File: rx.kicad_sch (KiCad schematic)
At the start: 33 parts, among them U1 CC1200

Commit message: MPN/PN update
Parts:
- C5: MPN (none) -> C0603C473K5RACTU
- C5: MPN (none) -> GRM1885C1H152JA01D
- C5: MPN (none) -> C0603C223K4RACTU
- C5: MPN (none) -> GRM1885C1H9R1BA01D
- C5: MPN (none) -> CC0603CRNPO9BN5R1
- C5: MPN (none) -> C0603C103K5RAC7081
- C5: MPN (none) -> C0603C104M5RAC7411
- C5: MPN (none) -> GRM1885C1H6R2BA01D
- FB1: MPN (none) -> BLM18KG601SH1D
- JP1, TP5: MPN (none) -> -
- L3: MPN (none) -> LQW18AS15NG00D; PN (none) -> LQW18AS15NG00D
- L3: MPN (none) -> LQW18AN27NG00D; PN (none) -> LQW18AN27NG00D
- L3: MPN (none) -> LQW18AN22NG00D; PN (none) -> LQW18AN22NG00D
- L3: MPN (none) -> LQW18AS56NG00D; PN (none) -> LQW18AS56NG00D
- R2: MPN (none) -> CRCW0603100RFKECC; PN (none) -> CRCW0603100RFKECC
- R2: MPN (none) -> CRGCQ0603F56K; PN (none) -> CRGCQ0603F56K
- U1: MPN (none) -> CC1200RHBR
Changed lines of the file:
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@@
+      (effects (font (size 1.27 1.27)) hide)
+    )
+    (property "MPN" "LQW18AS15NG00D" (at 228.6 134.62 0)
+      (effects (font (size 1.27 1.27)) hide)
+    )
+    (property "PN" "LQW18AS15NG00D" (at 228.6 134.62 0)
       (effects (font (size 1.27 1.27)) hide)
     )
@@
       (effects (font (size 1.27 1.27)) hide)
     )
+    (property "MPN" "C0603C473K5RACTU" (at 177.8 205.74 0)
+      (effects (font (size 1.27 1.27)) hide)
+    )
     (pin "1")
     (pin "2")
@@
       (effects (font (size 1.27 1.27)) hide)
     )
+    (property "MPN" "LQW18AN27NG00D" (at 213.36 128.27 0)
+      (effects (font (size 1.27 1.27)) hide)
+    )
+    (property "PN" "LQW18AN27NG00D" (at 213.36 128.27 0)
+      (effects (font (size 1.27 1.27)) hide)
+    )
     (pin "1")
     (pin "2")
@@
       (effects (font (size 1.27 1.27)) hide)
     )
+    (property "MPN" "C0603C473K5RACTU" (at 124.46 205.74 0)
+      (effects (font (size 1.27 1.27)) hide)
+    )
     (pin "1")
     (pin "2")
@@
     )
     (property "PN" "GRM1885C1H152JA01D" (at 152.4 106.68 0)
+      (effects (font (size 1.27 1.27)) hide)
+    )
+    (property "MPN" "GRM1885C1H152JA01D" (at 152.4 106.68 0)
       (effects (font (size 1.27 1.27)) hide)
     )
@@
       (effects (font (size 1.27 1.27)) hide)
     )
+    (property "MPN" "C0603C223K4RACTU" (at 247.65 101.6 0)
+      (effects (font (size 1.27 1.27)) hide)
+    )
     (pin "1")
     (pin "2")
@@
       (effects (font (size 1.27 1.27)) hide)
     )
+    (property "MPN" "C0603C473K5RACTU" (at 160.02 205.74 0)
+      (effects (font (size 1.27 1.27)) hide)
+    )
     (pin "1")
     (pin "2")
@@
       (effects (font (size 1.27 1.27)) hide)
     )
+    (property "MPN" "C0603C473K5RACTU" (at 195.58 205.74 0)
+      (effects (font (size 1.27 1.27)) hide)
+    )
     (pin "1")
     (pin "2")
@@
       (effects (font (size 1.27 1.27)) hide)
     )
+    (property "MPN" "-" (at 204.47 68.58 0)
+      (effects (font (size 1.27 1.27)) hide)
+    )
     (pin "1")
     (pin "2")
@@
       (effects (font (size 1.27 1.27)) hide)
     )
+    (property "MPN" "C0603C473K5RACTU" (at 219.71 101.6 0)
+      (effects (font (size 1.27 1.27)) hide)
+    )
     (pin "1")
     (pin "2")
@@
       (effects (font (size 1.27 1.27)) hide)
     )
+    (property "MPN" "GRM1885C1H9R1BA01D" (at 152.4 93.98 0)
+      (effects (font (size 1.27 1.27)) hide)
+    )
     (pin "1")
     (pin "2")
@@
       (effects (font (size 1.27 1.27)) hide)
     )
+    (property "MPN" "CC0603CRNPO9BN5R1" (at 203.2 128.27 0)
+      (effects (font (size 1.27 1.27)) hide)
+    )
     (pin "1")
     (pin "2")
@@
       (effects (font (size 1.27 1.27)) hide)
     )
+    (property "MPN" "LQW18AN22NG00D" (at 247.65 134.62 0)
+      (effects (font (size 1.27 1.27)) hide)
+    )
+    (property "PN" "LQW18AN22NG00D" (at 247.65 134.62 0)
+      (effects (font (size 1.27 1.27)) hide)
+    )
     (pin "1")
     (pin "2")
@@
       (effects (font (size 1.27 1.27)) hide)
     )
+    (property "MPN" "C0603C473K5RACTU" (at 186.69 205.74 0)
+      (effects (font (size 1.27 1.27)) hide)
+    )
     (pin "1")
     (pin "2")
@@
       (effects (font (size 1.27 1.27)) hide)
     )
+    (property "MPN" "C0603C473K5RACTU" (at 142.24 205.74 0)
+      (effects (font (size 1.27 1.27)) hide)
+    )
     (pin "1")
     (pin "2")
@@
       (effects (font (size 1.27 1.27)) hide)
     )
+    (property "MPN" "C0603C473K5RACTU" (at 133.35 205.74 0)
+      (effects (font (size 1.27 1.27)) hide)
+    )
     (pin "1")
     (pin "2")
@@
       (effects (font (size 1.27 1.27)) hide)
     )
+    (property "MPN" "C0603C103K5RAC7081" (at 237.49 101.6 0)
+      (effects (font (size 1.27 1.27)) hide)
+    )
     (pin "1")
     (pin "2")
@@
       (effects (font (size 1.27 1.27)) hide)
     )
+    (property "MPN" "CC0603CRNPO9BN5R1" (at 219.71 127 0)
+      (effects (font (size 1.27 1.27)) hide)
+    )
     (pin "1")
     (pin "2")
@@
       (effects (font (size 1.27 1.27)) hide)
     )
-    (property "PN" "" (at 152.4 71.12 0)
+    (property "PN" "CRCW0603100RFKECC" (at 152.4 71.12 0)
+      (effects (font (size 1.27 1.27)) hide)
+    )
+    (property "MPN" "CRCW0603100RFKECC" (at 152.4 71.12 0)
       (effects (font (size 1.27 1.27)) hide)
     )
@@
       (effects (font (size 1.27 1.27)) hide)
     )
-    (property "PN" "" (at 152.4 73.66 0)
+    (property "PN" "CRCW0603100RFKECC" (at 152.4 73.66 0)
+      (effects (font (size 1.27 1.27)) hide)
+    )
+    (property "MPN" "CRCW0603100RFKECC" (at 152.4 73.66 0)
       (effects (font (size 1.27 1.27)) hide)
     )
@@
       (effects (font (size 1.27 1.27)) hide)
     )
+    (property "MPN" "C0603C104M5RAC7411" (at 207.01 205.74 0)
+      (effects (font (size 1.27 1.27)) hide)
+    )
     (pin "1")
     (pin "2")
@@
       (effects (font (size 1.27 1.27)) hide)
     )
+    (property "MPN" "C0603C473K5RACTU" (at 168.91 205.74 0)
+      (effects (font (size 1.27 1.27)) hide)
+    )
     (pin "1")
     (pin "2")
@@
       (effects (font (size 1.27 1.27)) hide)
     )
+    (property "MPN" "CC0603CRNPO9BN5R1" (at 237.49 134.62 0)
+      (effects (font (size 1.27 1.27)) hide)
+    )
     (pin "1")
     (pin "2")
@@
       (effects (font (size 1.27 1.27)) hide)
     )
+    (property "MPN" "LQW18AS56NG00D" (at 208.28 123.19 0)
+      (effects (font (size 1.27 1.27)) hide)
+    )
+    (property "PN" "LQW18AS56NG00D" (at 208.28 123.19 0)
+      (effects (font (size 1.27 1.27)) hide)
+    )
     (pin "1")
     (pin "2")
@@
       (effects (font (size 1.27 1.27)) hide)
     )
-    (property "PN" "" (at 152.4 99.06 0)
+    (property "PN" "CRGCQ0603F56K" (at 152.4 99.06 0)
+      (effects (font (size 1.27 1.27)) hide)
+    )
+    (property "MPN" "CRGCQ0603F56K" (at 152.4 99.06 0)
       (effects (font (size 1.27 1.27)) hide)
     )
@@
       (effects (font (size 1.27 1.27)) hide)
     )
+    (property "MPN" "GRM1885C1H6R2BA01D" (at 242.57 139.7 0)
+      (effects (font (size 1.27 1.27)) hide)
+    )
     (pin "1")
     (pin "2")
@@
       (effects (font (size 1.27 1.27)) hide)
     )
+    (property "MPN" "LQW18AN27NG00D" (at 196.85 127 0)
+      (effects (font (size 1.27 1.27)) hide)
+    )
+    (property "PN" "LQW18AN27NG00D" (at 196.85 127 0)
+      (effects (font (size 1.27 1.27)) hide)
+    )
     (pin "1")
     (pin "2")
@@
       (effects (font (size 1.27 1.27)) hide)
     )
+    (property "MPN" "-" (at 147.32 91.44 0)
+      (effects (font (size 1.27 1.27)) hide)
+    )
     (pin "1")
     (instances
@@
       (effects (font (size 1.27 1.27)) hide)
     )
+    (property "MPN" "C0603C473K5RACTU" (at 228.6 101.6 0)
+      (effects (font (size 1.27 1.27)) hide)
+    )
     (pin "1")
     (pin "2")
@@
     )
     (property "PN" "CC1200RHBR" (at 176.53 86.36 0)
+      (effects (font (size 1.27 1.27)) hide)
+    )
+    (property "MPN" "CC1200RHBR" (at 176.53 86.36 0)
       (effects (font (size 1.27 1.27)) hide)
     )
@@
       (effects (font (size 1.27 1.27)) hide)
     )
+    (property "MPN" "BLM18KG601SH1D" (at 201.93 200.66 0)
+      (effects (font (size 1.27 1.27)) hide)
+    )
     (pin "1")
     (pin "2")
@@
       (effects (font (size 1.27 1.27)) hide)
     )
-    (property "PN" "" (at 152.4 68.58 0)
+    (property "PN" "CRCW0603100RFKECC" (at 152.4 68.58 0)
+      (effects (font (size 1.27 1.27)) hide)
+    )
+    (property "MPN" "CRCW0603100RFKECC" (at 152.4 68.58 0)
       (effects (font (size 1.27 1.27)) hide)
     )
@@
       (effects (font (size 1.27 1.27)) hide)
     )
+    (property "MPN" "C0603C473K5RACTU" (at 151.13 205.74 0)
+      (effects (font (size 1.27 1.27)) hide)
+    )

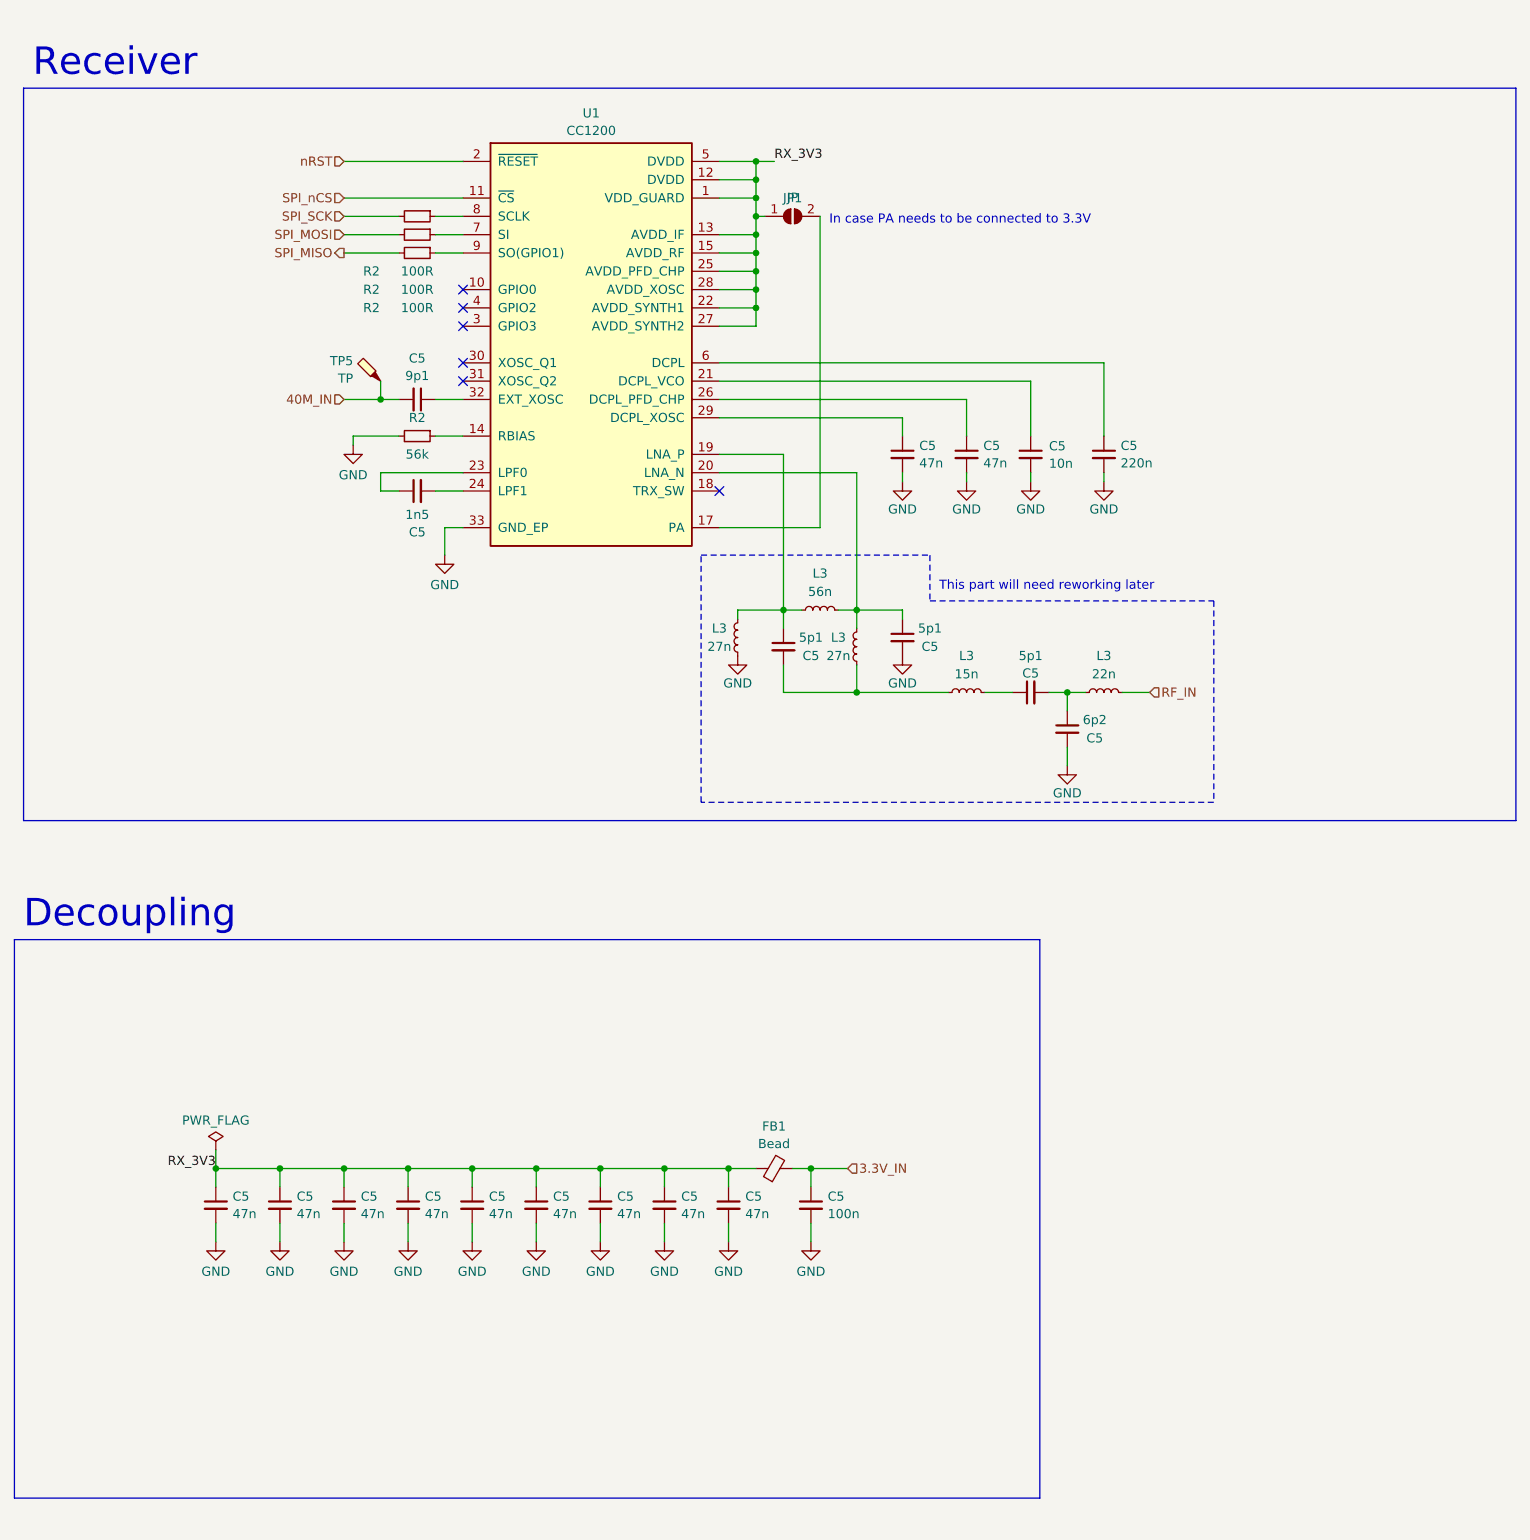
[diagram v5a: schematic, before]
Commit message: WIP rev B
- added bleed resistors
- power supply now uses linear regulators
- routed RX_SAMP_CLK
- added some decoupling at RF_PA_VDD
- added some GND vias here and there
- updated BOM
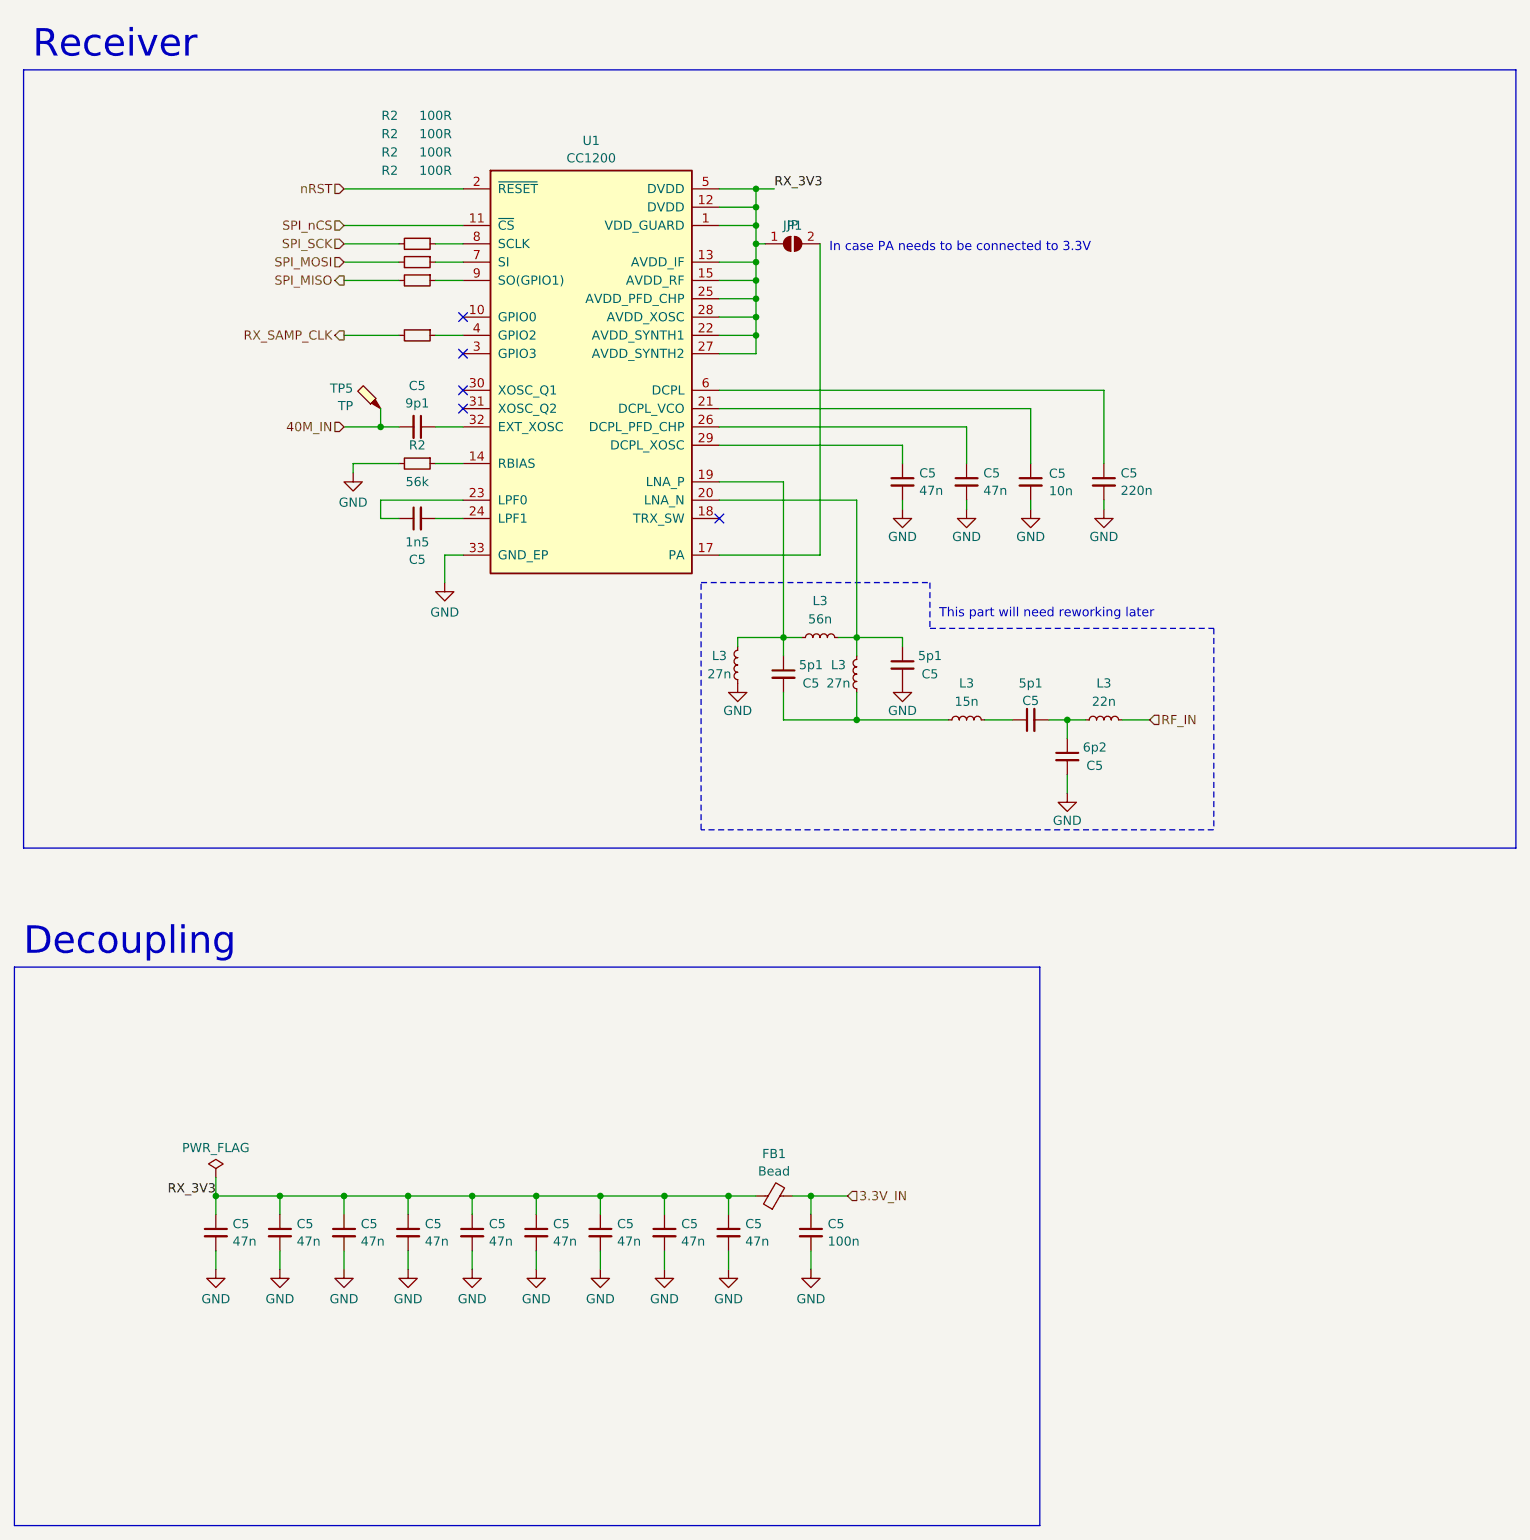
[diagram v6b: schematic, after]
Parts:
- added R2: 100R, Resistor_SMD:R_0603_1608Metric, symbol Device:R_Small
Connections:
- net at U1.4 (GPIO2): now also R2.1
- new net RX_SAMP_CLK: R2.2
- no-connect marks 6 -> 5
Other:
- moved on the sheet: C5, FB1, JP1, L3, R2, TP5, U1

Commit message: L1, L6 - PN update
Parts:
- L3: MPN LQW18AS56NG00D -> 81-LQW18AN56NG00D; PN LQW18AS56NG00D -> 81-LQW18AN56NG00D
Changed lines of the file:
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@@
       (effects (font (size 1.27 1.27)) hide)
     )
-    (property "MPN" "LQW18AS56NG00D" (at 208.28 127 0)
+    (property "MPN" "81-LQW18AN56NG00D" (at 208.28 127 0)
       (effects (font (size 1.27 1.27)) hide)
     )
-    (property "PN" "LQW18AS56NG00D" (at 208.28 127 0)
+    (property "PN" "81-LQW18AN56NG00D" (at 208.28 127 0)
       (effects (font (size 1.27 1.27)) hide)
     )
